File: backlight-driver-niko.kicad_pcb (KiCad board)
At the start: 2 copper layers, 20.8 x 26.8 mm, 14 parts

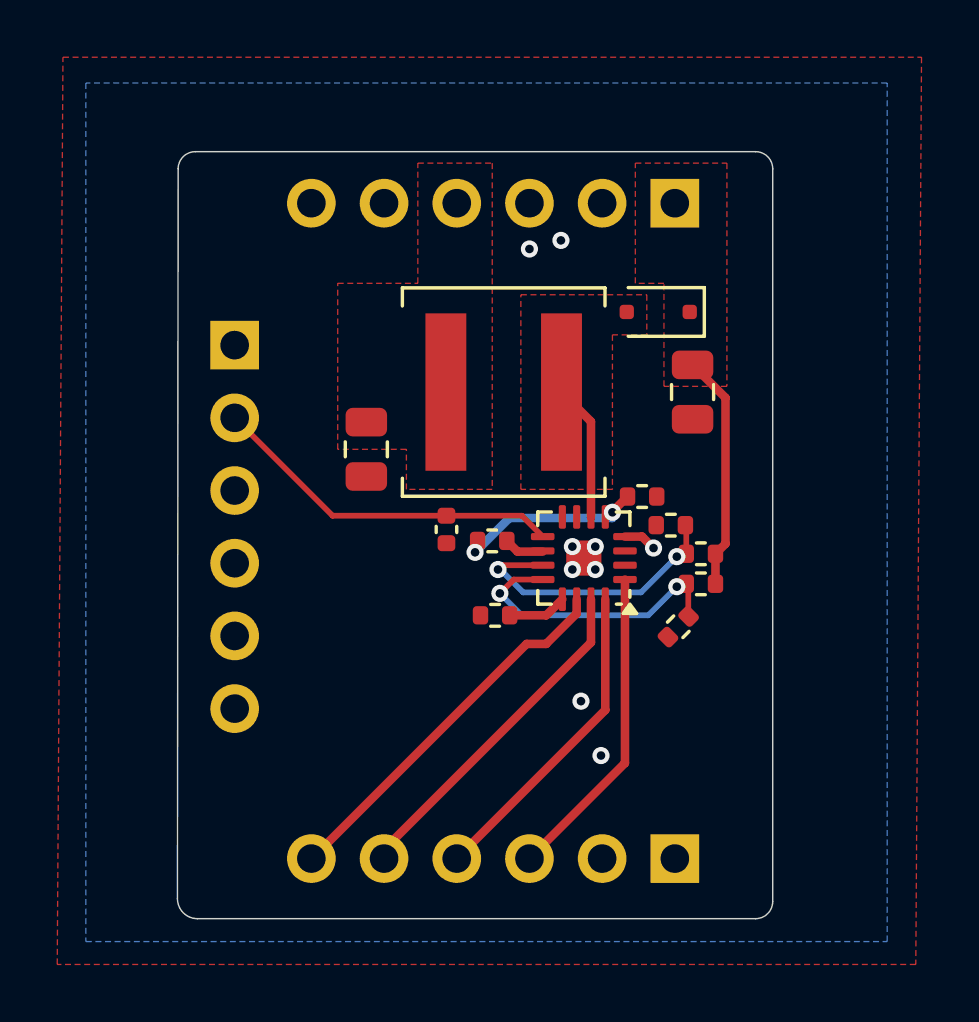
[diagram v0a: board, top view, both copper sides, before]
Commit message: Nikolite reviewed, silkscreen improved, added fuse, fixed a few small things wrt layout/sch
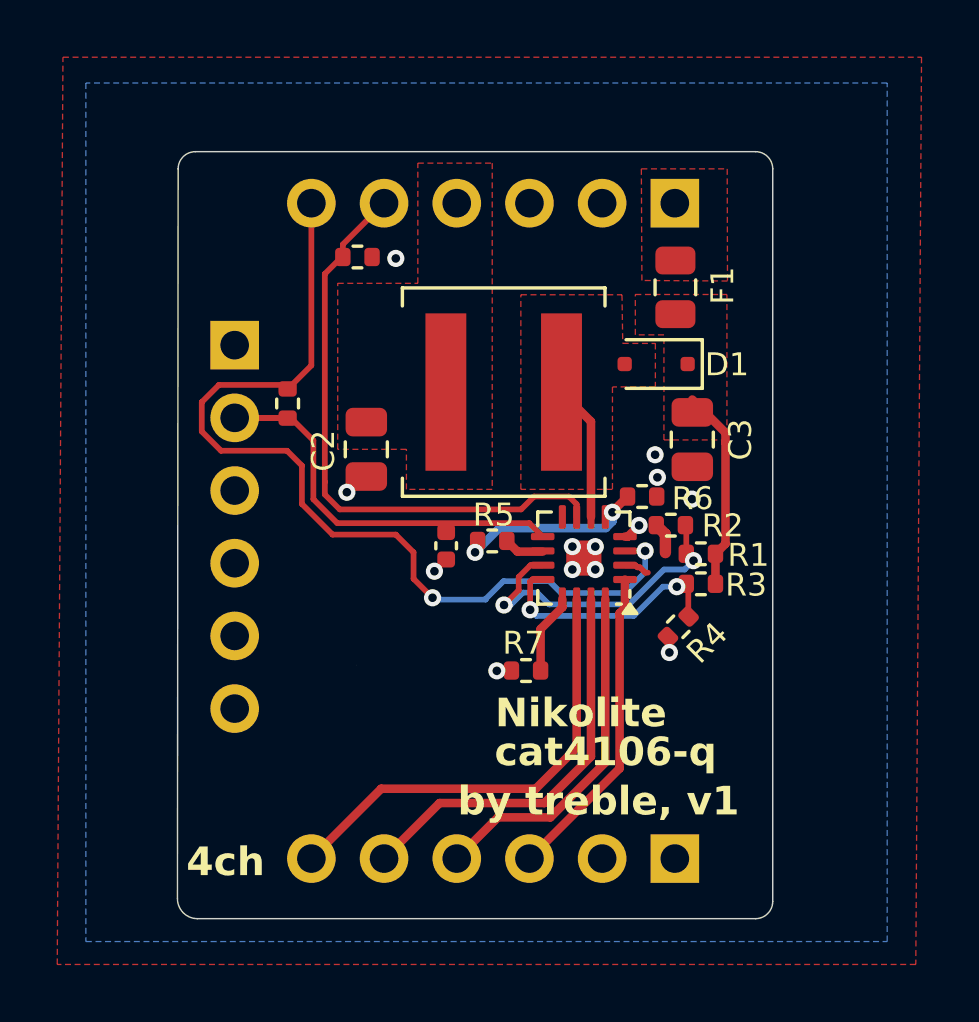
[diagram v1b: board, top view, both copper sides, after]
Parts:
- added F1: BL_Fuse, Fuse:Fuse_0805_2012Metric, F.Cu at (161.6, 89.5)
- added G***: LOGO, LOGO, F.Cu at (152.5, 103.5)
- added G***: LOGO, LOGO, B.Cu at (154.3, 93.6)
- added G***: LOGO, LOGO, B.Cu at (152.0, 101.9)
- added R8: 20K, Resistor_SMD:R_0402_1005Metric, F.Cu at (150.5, 88.5)
- added R9: 20K, Resistor_SMD:R_0402_1005Metric, F.Cu at (148.1, 93.6)
- C3: value 22uF -> 1uF
- R1: value R -> 430K
- R2, R4, R5, R6: value R -> 20K
- R3: value R -> 560K
- R7: value 4.7K -> 5.1K
- moved R7 2.21 mm to (156.4, 102.9)
- moved D1 1.82 mm to (160.9, 92.2)
- moved C3 1.66 mm to (162.2, 94.9)
- moved C1 0.57 mm to (153.6, 98.6)
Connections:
- J1 pad 1: VAD -> Net-(J1-VAD)
- J1 pad 3: unconnected-(J1-PWM-Pad3) -> L_PWM
- J1 pad 4: unconnected-(J1-Enable-Pad4) -> L_FAULT
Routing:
- net L_FAULT: track 0.00 -> 32.6 mm, vias 0 -> 2
- net L_PWM: track 0.00 -> 20.8 mm
- net +3V3: track 12.5 -> 15.5 mm
- net VCD4: track 13.3 -> 16.1 mm
- net VCD3: track 12.1 -> 14.2 mm
- net L_VFMAX: track 9.95 -> 8.43 mm
- net GND: track 1.16 -> 2.66 mm, vias 9 -> 13
- net VAD: track 8.27 -> 7.07 mm
- net VCD2: track 11.2 -> 12.3 mm
- net L_VFMIN: track 10.1 -> 11.2 mm
- net Net-(U1-RSET): track 2.07 -> 2.81 mm
- added copper zone on F.Cu, net Net-(J1-VAD)
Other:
- board text added: "3V3"
- board text added: "4ch"
- board text added: "C1"
- board text added: "C2"
- board text added: "C3"
- board text added: "C4"
- board text added: "FLT"
- board text added: "GND"
- board text added: "Nikolite"
- board text added: "PWM"
- board text added: "VAD"
- board text added: "VIN"
- board text added: "X"
- board text added: "by treble, v1"
- board text added: "cat4106-q"
- board text added: "nc"
- board text added: "trans rights"
